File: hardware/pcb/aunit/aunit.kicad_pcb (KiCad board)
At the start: 2 copper layers, 62.2 x 21.6 mm, 48 parts, among them J1 BUS, J2 Input A, J3 Input B, J4 Control, J5 Flags, J6 Power, U1 74HC283, U2 74HC283, U3 74HC86, U4 74HC86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

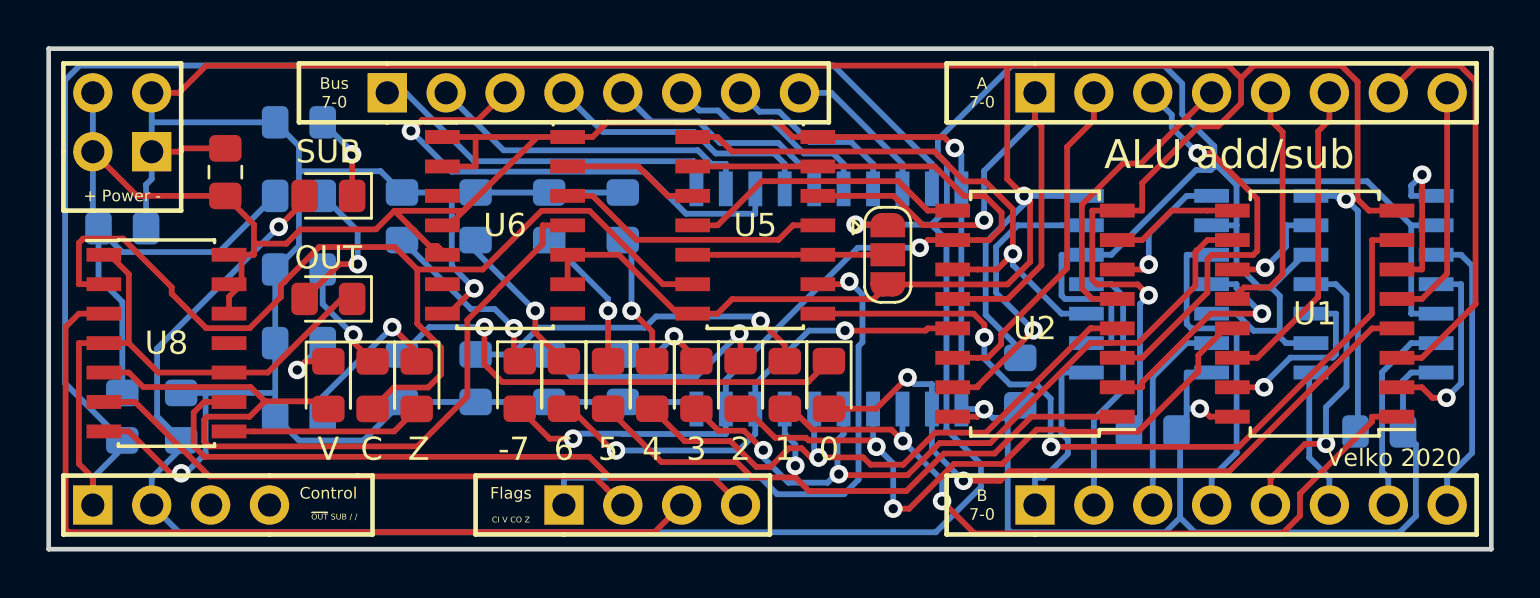
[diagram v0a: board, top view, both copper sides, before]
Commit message: Add copper pours and remove redundant tracks
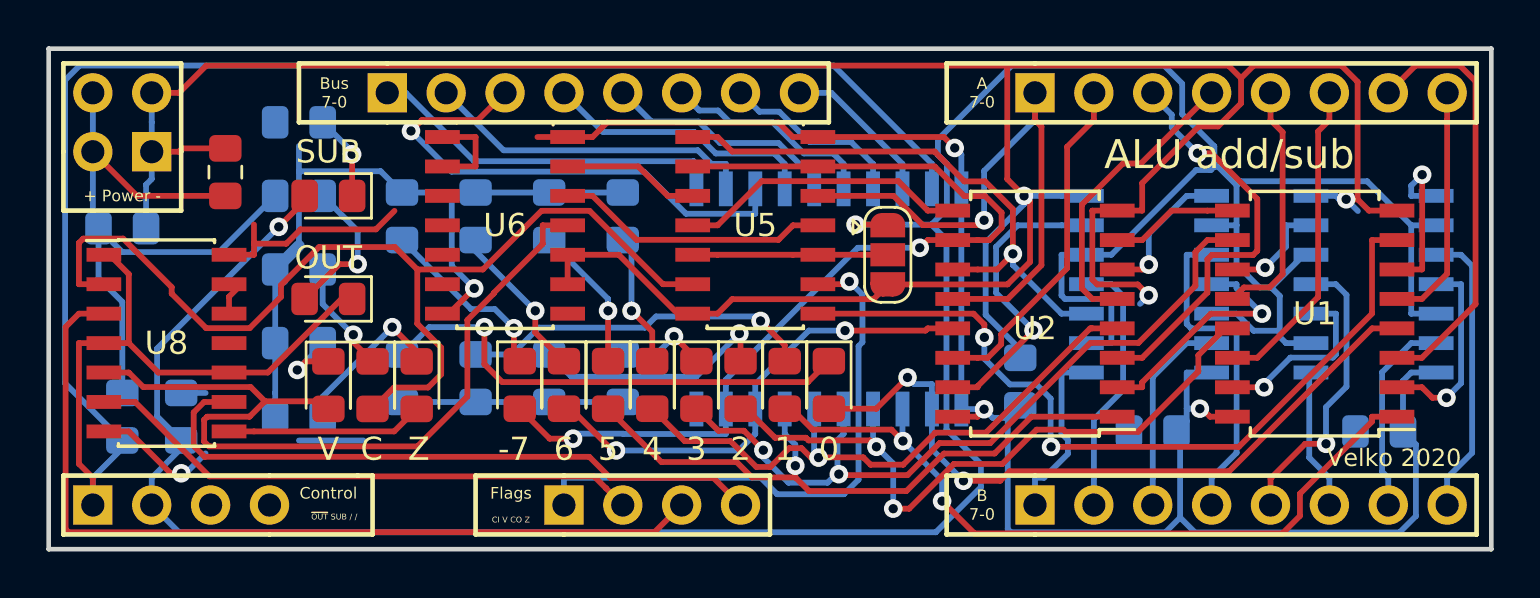
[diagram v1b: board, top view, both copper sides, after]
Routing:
- net GND: track 217.9 -> 184.0 mm
- net VCC: track 137.0 -> 119.8 mm
- added copper zone on B.Cu, net GND
- added copper zone on F.Cu, net VCC

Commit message: Silkscreen documentation
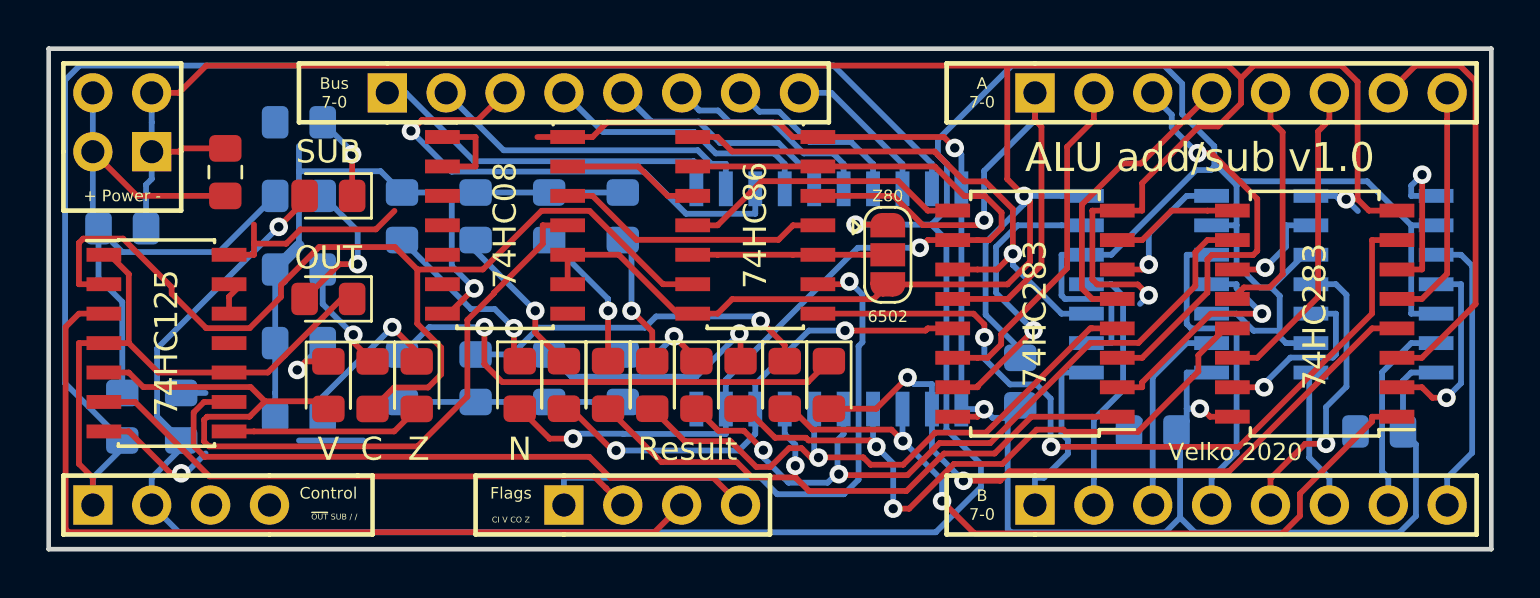
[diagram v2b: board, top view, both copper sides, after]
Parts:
- D3: value 3 -> Result
- D7: value -7 -> N
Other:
- board text added: "6502"
- board text added: "ALU add/sub v1.0"
- board text added: "LED resistors"
- board text added: "Z80"
- board text added: "pull"
- board text removed: "ALU add/sub"

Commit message: Silk/via corrections
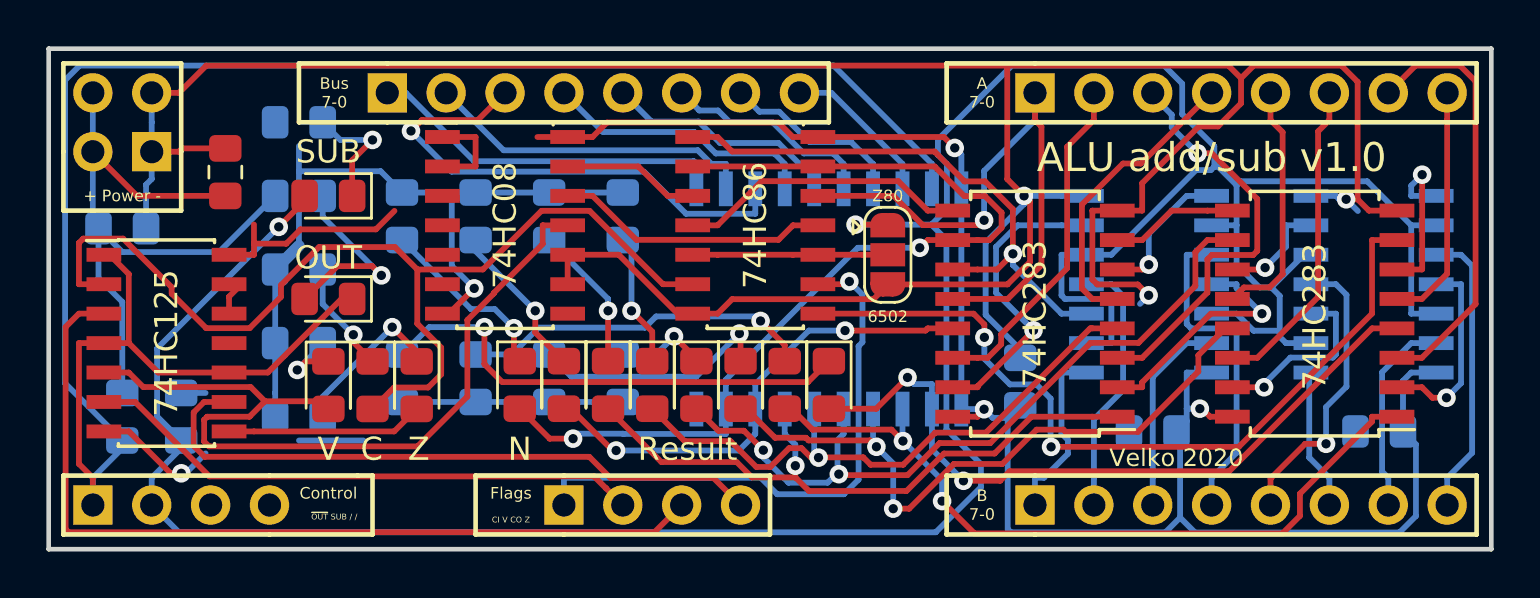
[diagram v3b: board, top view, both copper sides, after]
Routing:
- net Net-(D8-Pad2): track 6.48 -> 8.54 mm
- net Net-(D11-Pad1): track 3.70 -> 5.24 mm
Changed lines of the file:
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@@
-(kicad_pcb (version 20171130) (host pcbnew "(5.1.6)-1")
+(kicad_pcb (version 20171130) (host pcbnew 5.0.2+dfsg1-1)
   (general
     (thickness 1.6)
     (drawings 67)
-    (tracks 821)
+    (tracks 823)
     (zones 0)
     (modules 48)
@@
   (page A4)
   (layers
-    (0 F.Cu signal hide)
+    (0 F.Cu signal)
     (31 B.Cu signal hide)
     (32 B.Adhes user hide)
@@
     (zone_45_only no)
     (trace_min 0.2)
+    (segment_width 0.2)
+    (edge_width 0.1)
     (via_size 0.8)
     (via_drill 0.4)
@@
     (uvia_min_size 0.2)
     (uvia_min_drill 0.1)
-    (edge_width 0.1)
-    (segment_width 0.2)
     (pcb_text_width 0.3)
     (pcb_text_size 1.5 1.5)
@@
     (effects (font (size 0.5 0.5) (thickness 0.1)))
   )
-  (gr_text "Velko 2020" (at 86.106 53.594) (layer F.SilkS)
+  (gr_text "Velko 2020" (at 83.566 53.848) (layer F.SilkS)
     (effects (font (size 0.75 0.75) (thickness 0.1875)))
   )
-  (gr_text "ALU add/sub v1.0" (at 84.582 40.894) (layer F.SilkS)
+  (gr_text "ALU add/sub v1.0" (at 85.09 40.894) (layer F.SilkS)
     (effects (font (size 1.25 1.25) (thickness 0.3)))
   )
@@
   (segment (start 46.745 47.2121) (end 48.0658 48.5329) (width 0.25) (layer B.Cu) (net 23))
   (via (at 48.0658 48.5329) (size 0.8) (layers F.Cu B.Cu) (net 23))
-  (segment (start 48.015 42.545) (end 48.015 40.7486) (width 0.25) (layer F.Cu) (net 24))
-  (segment (start 46.745 39.37) (end 48.015 40.64) (width 0.25) (layer B.Cu) (net 24))
-  (segment (start 48.015 40.64) (end 48.015 40.7486) (width 0.25) (layer B.Cu) (net 24))
-  (via (at 48.015 40.7486) (size 0.8) (layers F.Cu B.Cu) (net 24))
+  (via (at 48.895 40.132) (size 0.8) (layers F.Cu B.Cu) (net 24))
+  (segment (start 47.507 40.132) (end 46.745 39.37) (width 0.25) (layer B.Cu) (net 24))
+  (segment (start 48.895 40.132) (end 47.507 40.132) (width 0.25) (layer B.Cu) (net 24))
+  (segment (start 48.015 41.012) (end 48.015 42.545) (width 0.25) (layer F.Cu) (net 24))
+  (segment (start 48.895 40.132) (end 48.015 41.012) (width 0.25) (layer F.Cu) (net 24))
   (segment (start 87.663 46.4945) (end 88.0281 46.8596) (width 0.25) (layer B.Cu) (net 25))
   (segment (start 88.0281 46.8596) (end 88.0281 48.3615) (width 0.25) (layer B.Cu) (net 25))
@@
   (segment (start 62.705 45.085) (end 63.7803 45.085) (width 0.25) (layer F.Cu) (net 73))
   (segment (start 68.105 45.085) (end 67.0297 45.085) (width 0.25) (layer F.Cu) (net 73))
-  (segment (start 48.2547 45.4898) (end 48.2547 44.0547) (width 0.25) (layer B.Cu) (net 74))
-  (segment (start 48.2547 44.0547) (end 46.745 42.545) (width 0.25) (layer B.Cu) (net 74))
-  (segment (start 45.965 46.99) (end 47.4652 45.4898) (width 0.25) (layer F.Cu) (net 74))
-  (segment (start 47.4652 45.4898) (end 48.2547 45.4898) (width 0.25) (layer F.Cu) (net 74))
-  (via (at 48.2547 45.4898) (size 0.8) (layers F.Cu B.Cu) (net 74))
+  (via (at 49.276 45.974) (size 0.8) (layers F.Cu B.Cu) (net 74))
+  (segment (start 46.745 43.443) (end 46.745 42.545) (width 0.25) (layer B.Cu) (net 74))
+  (segment (start 49.276 45.974) (end 46.745 43.443) (width 0.25) (layer B.Cu) (net 74))
+  (segment (start 48.876001 45.574001) (end 49.276 45.974) (width 0.25) (layer F.Cu) (net 74))
+  (segment (start 47.380999 45.574001) (end 48.876001 45.574001) (width 0.25) (layer F.Cu) (net 74))
+  (segment (start 45.965 46.99) (end 47.380999 45.574001) (width 0.25) (layer F.Cu) (net 74))
   (zone (net 2) (net_name GND) (layer B.Cu) (hatch edge 0.508)
     (connect_pads (clearance 0.208))

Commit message: AU pwr_in cap value
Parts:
- C1: value 100nF -> 10μF
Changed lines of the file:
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@@
       (effects (font (size 1 1) (thickness 0.15)) (justify mirror))
     )
-    (fp_text value 100nF (at 0 -1.65) (layer B.Fab)
+    (fp_text value 10μF (at 0 1.778) (layer B.SilkS)
       (effects (font (size 1 1) (thickness 0.15)) (justify mirror))
     )
